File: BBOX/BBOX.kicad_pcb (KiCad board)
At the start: 2 copper layers, 47 x 42.7 mm, 20 parts, among them J1 BBOX, J10 LED, J2 WJ127-5.0-2P, J3 Servo2, J7 IR_LEDs, J9 Servo1, Q1 IRLML2502PBF, U2 AP2210N-3.3TRG1, U4 PCA9685PW, U5 PCA9306

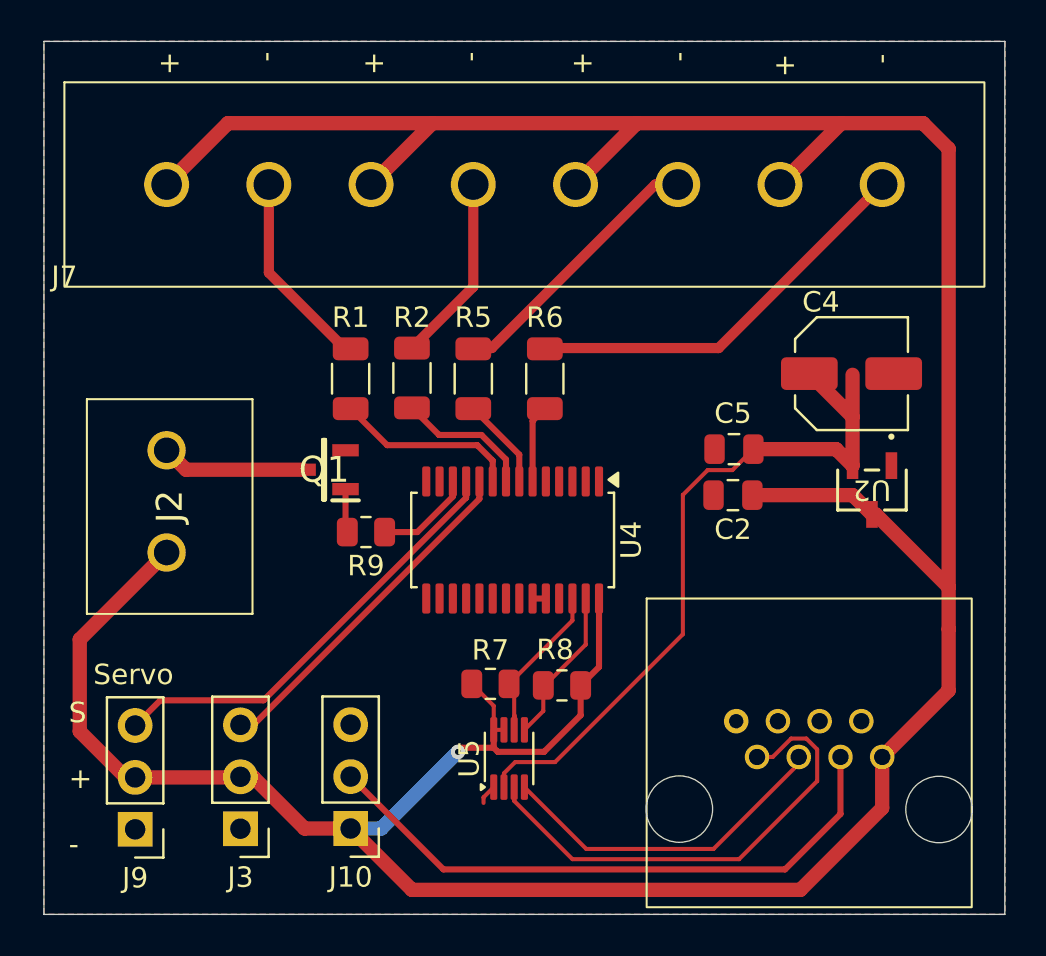
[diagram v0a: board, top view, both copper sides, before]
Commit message: Adding fuseholder to the HAT
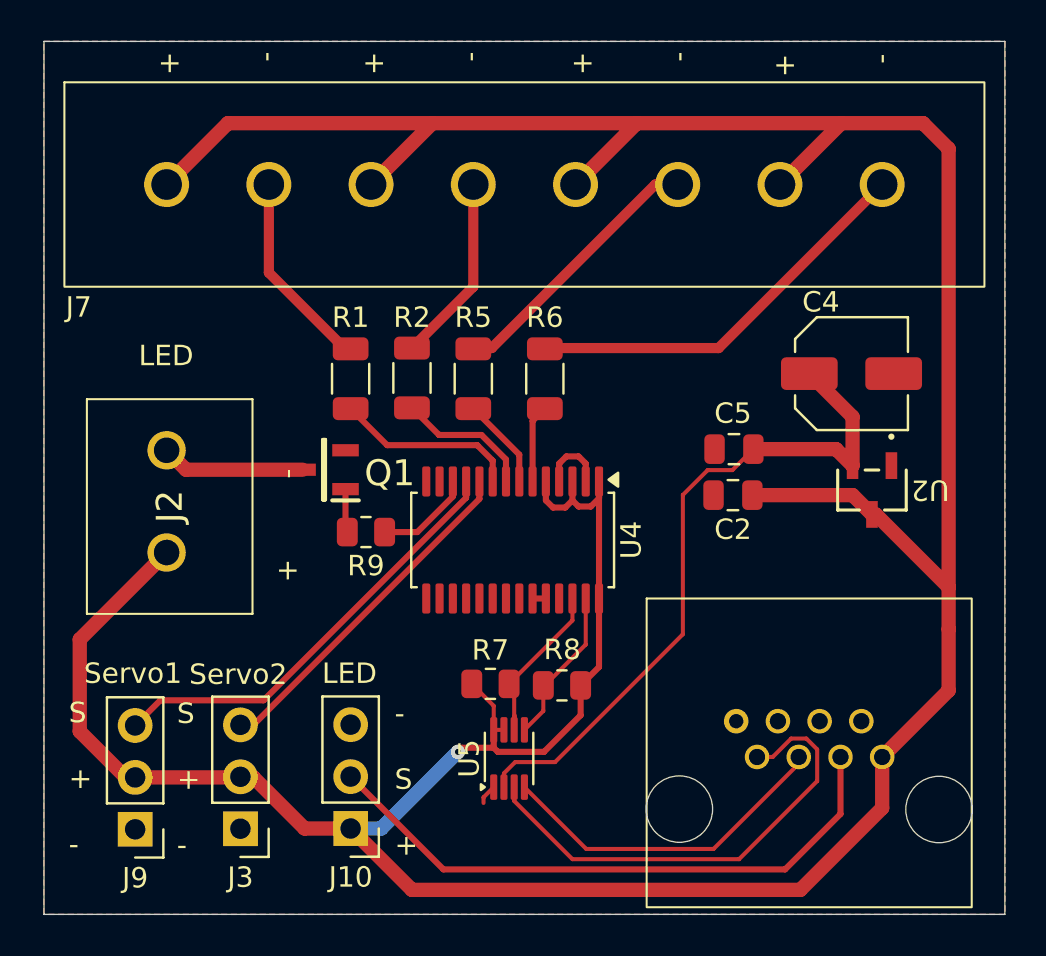
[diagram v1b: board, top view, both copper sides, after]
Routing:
- net +VDC: track 176.3 -> 187.9 mm
- net GND: track 1.63 -> 4.97 mm
- net +3.3VA: track 36.1 -> 34.0 mm
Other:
- board text added: "+ -"
- board text added: "- S +"
- board text added: "LED"
- board text added: "Servo1"
- board text added: "Servo2"
- board text removed: "Servo"
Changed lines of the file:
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@@
 		(tags "MOSFET (N-Channel)")
 		(property "Reference" "Q1"
-			(at 0 0 0)
+			(at -3.21 -0.17 0)
 			(layer "F.SilkS")
 			(effects
@@
 		(tags "AP2210N-3.3TRG1 ")
 		(property "Reference" "U2"
-			(at 0 0 180)
+			(at -2.85 0 180)
 			(unlocked yes)
 			(layer "F.SilkS")
@@
 		(tags "resistor")
 		(property "Reference" "R8"
-			(at 0.3375 1.75 0)
+			(at -0.0125 1.75 0)
 			(layer "F.SilkS")
 			(effects
@@
 		(at 141 77)
 		(property "Reference" "J7"
-			(at 0 -0.5 0)
+			(at 0.7 1 0)
 			(unlocked yes)
 			(layer "F.SilkS")
@@
 		)
 	)
-	(gr_text "Servo"
-		(at 142.41 96.56 0)
+	(gr_text "Servo1"
+		(at 141.95 96.5 0)
+		(layer "F.SilkS")
+		(effects
+			(font
+				(size 1 1)
+				(thickness 0.1)
+			)
+			(justify left bottom)
+		)
+	)
+	(gr_text "LED"
+		(at 144.63 80.96 0)
+		(layer "F.SilkS")
+		(effects
+			(font
+				(size 1 1)
+				(thickness 0.1)
+			)
+			(justify left bottom)
+		)
+	)
+	(gr_text "S\n\n+\n\n-"
+		(at 146.5 104.9 0)
+		(layer "F.SilkS")
+		(effects
+			(font
+				(size 1 1)
+				(thickness 0.1)
+			)
+			(justify left bottom)
+		)
+	)
+	(gr_text "Servo2"
+		(at 147.1 96.55 0)
+		(layer "F.SilkS")
+		(effects
+			(font
+				(size 1 1)
+				(thickness 0.1)
+			)
+			(justify left bottom)
+		)
+	)
+	(gr_text "LED"
+		(at 153.6 96.5 0)
+		(layer "F.SilkS")
+		(effects
+			(font
+				(size 1 1)
+				(thickness 0.1)
+			)
+			(justify left bottom)
+		)
+	)
+	(gr_text "-\n\nS\n\n+"
+		(at 157.15 104.9 0)
+		(layer "F.SilkS")
+		(effects
+			(font
+				(size 1 1)
+				(thickness 0.1)
+			)
+			(justify left bottom)
+		)
+	)
+	(gr_text "+         -"
+		(at 152.48 91.46 90)
 		(layer "F.SilkS")
 		(effects
@@
 	)
 	(segment
+		(start 165.2 86.525)
+		(end 165.2 85.65)
+		(width 0.3)
+		(layer "F.Cu")
+		(net 1)
+	)
+	(segment
+		(start 166.15 85.3)
+		(end 166.5 85.65)
+		(width 0.3)
+		(layer "F.Cu")
+		(net 1)
+	)
+	(segment
 		(start 161.5 101.975)
 		(end 161.5 102.25)
@@
 	)
 	(segment
+		(start 166.5 85.65)
+		(end 166.5 86.525)
+		(width 0.3)
+		(layer "F.Cu")
+		(net 1)
+	)
+	(segment
+		(start 165.2 85.65)
+		(end 165.55 85.3)
+		(width 0.3)
+		(layer "F.Cu")
+		(net 1)
+	)
+	(segment
 		(start 164.55 92.25)
 		(end 163.9 92.25)
@@
 	)
 	(segment
+		(start 165.55 85.3)
+		(end 166.15 85.3)
+		(width 0.3)
+		(layer "F.Cu")
+		(net 1)
+	)
+	(segment
 		(start 162 99.55)
 		(end 162 98.675)
@@
 	)
 	(segment
+		(start 167.15 92.25)
+		(end 167.15 86.525)
+		(width 0.3)
+		(layer "F.Cu")
+		(net 2)
+	)
+	(segment
 		(start 166.25 96.5)
 		(end 166.25 97.960572)
@@
 	)
 	(segment
+		(start 165.5 87.8)
+		(end 165.85 87.45)
+		(width 0.3)
+		(layer "F.Cu")
+		(net 2)
+	)
+	(segment
 		(start 146 90)
 		(end 141.75 94.25)
@@
 	)
 	(segment
+		(start 167.15 86.525)
+		(end 167.15 87.35)
+		(width 0.3)
+		(layer "F.Cu")
+		(net 2)
+	)
+	(segment
 		(start 164.460572 99.75)
 		(end 162.2 99.75)
@@
 	)
 	(segment
+		(start 166.15 87.75)
+		(end 165.85 87.45)
+		(width 0.3)
+		(layer "F.Cu")
+		(net 2)
+	)
+	(segment
+		(start 165.85 87.45)
+		(end 165.85 86.525)
+		(width 0.3)
+		(layer "F.Cu")
+		(net 2)
+	)
+	(segment
+		(start 167.15 87.35)
+		(end 166.75 87.75)
+		(width 0.3)
+		(layer "F.Cu")
+		(net 2)
+	)
+	(segment
 		(start 144 101)
 		(end 144.46 101)
@@
 	)
 	(segment
+		(start 164.55 87.45)
+		(end 164.9 87.8)
+		(width 0.3)
+		(layer "F.Cu")
+		(net 2)
+	)
+	(segment
 		(start 176 72)
 		(end 179 69)
@@
 	)
 	(segment
+		(start 164.9 87.8)
+		(end 165.5 87.8)
+		(width 0.3)
+		(layer "F.Cu")
+		(net 2)
+	)
+	(segment
 		(start 179 69)
 		(end 169 69)
@@
 	)
 	(segment
+		(start 164.55 86.525)
+		(end 164.55 87.45)
+		(width 0.3)
+		(layer "F.Cu")
+		(net 2)
+	)
+	(segment
 		(start 184.25 93.75)
 		(end 184.25 70.25)
@@
 		(net 2)
 	)
+	(segment
+		(start 166.75 87.75)
+		(end 166.15 87.75)
+		(width 0.3)
+		(layer "F.Cu")
+		(net 2)
+	)
 	(via
 		(at 160.25 99.75)
@@
 	(segment
 		(start 179.549999 83.362499)
-		(end 177.4375 81.25)
+		(end 179.549999 85.75)
 		(width 0.7)
 		(layer "F.Cu")
@@
 	)
 	(segment
-		(start 178.743799 84.9438)
-		(end 179.549999 85.75)
+		(start 179.549999 83.362499)
+		(end 177.4375 81.25)
 		(width 0.7)
 		(layer "F.Cu")
@@
 	)
 	(segment
-		(start 179.549999 85.75)
-		(end 179.549999 81.306299)
+		(start 178.743799 84.9438)
+		(end 179.549999 85.75)
 		(width 0.7)
 		(layer "F.Cu")
